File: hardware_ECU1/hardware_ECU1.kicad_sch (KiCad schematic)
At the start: 5 parts, among them J1 Micro_SD_Card, J2 VBAT circuit, U1 MPU-6050, U2 ESP32-WROOM-32

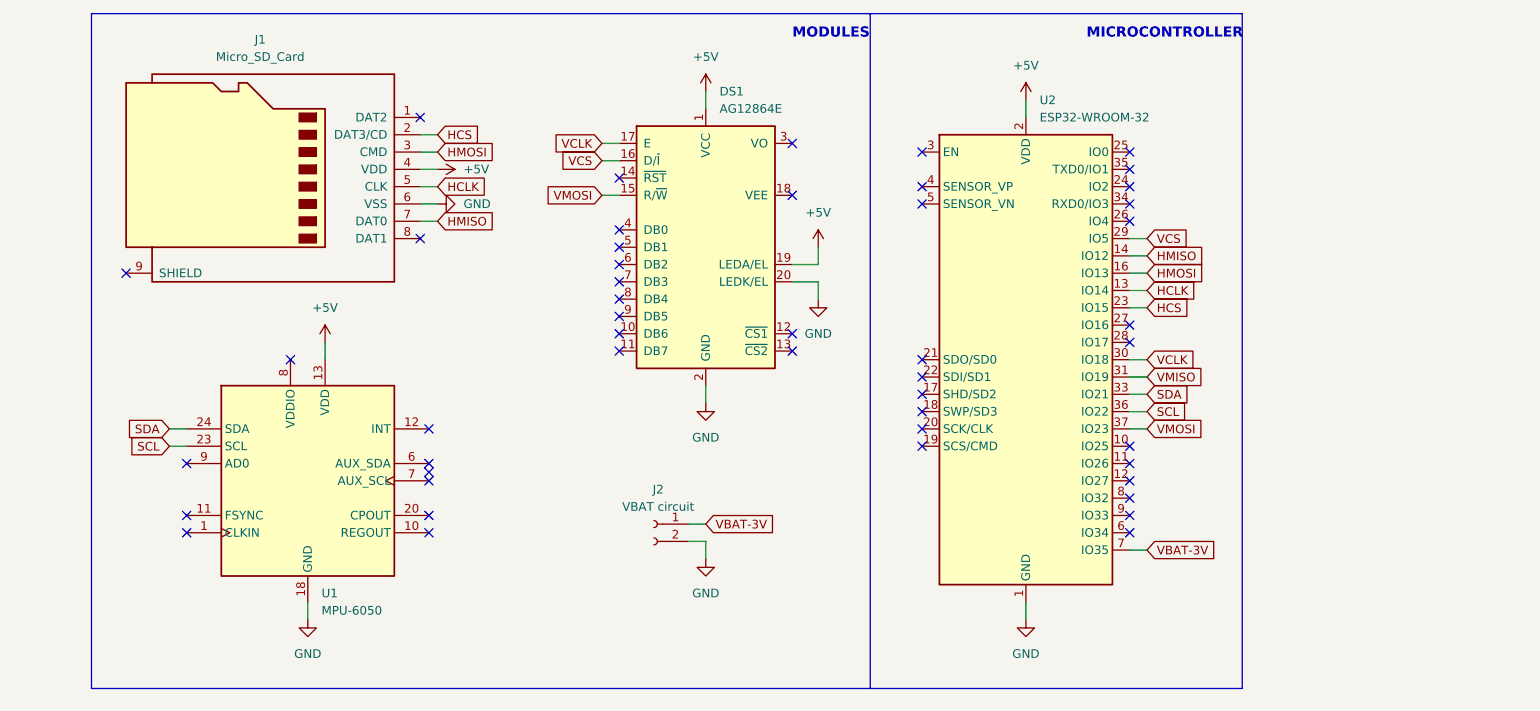
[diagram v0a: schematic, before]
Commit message: add buck to schematic
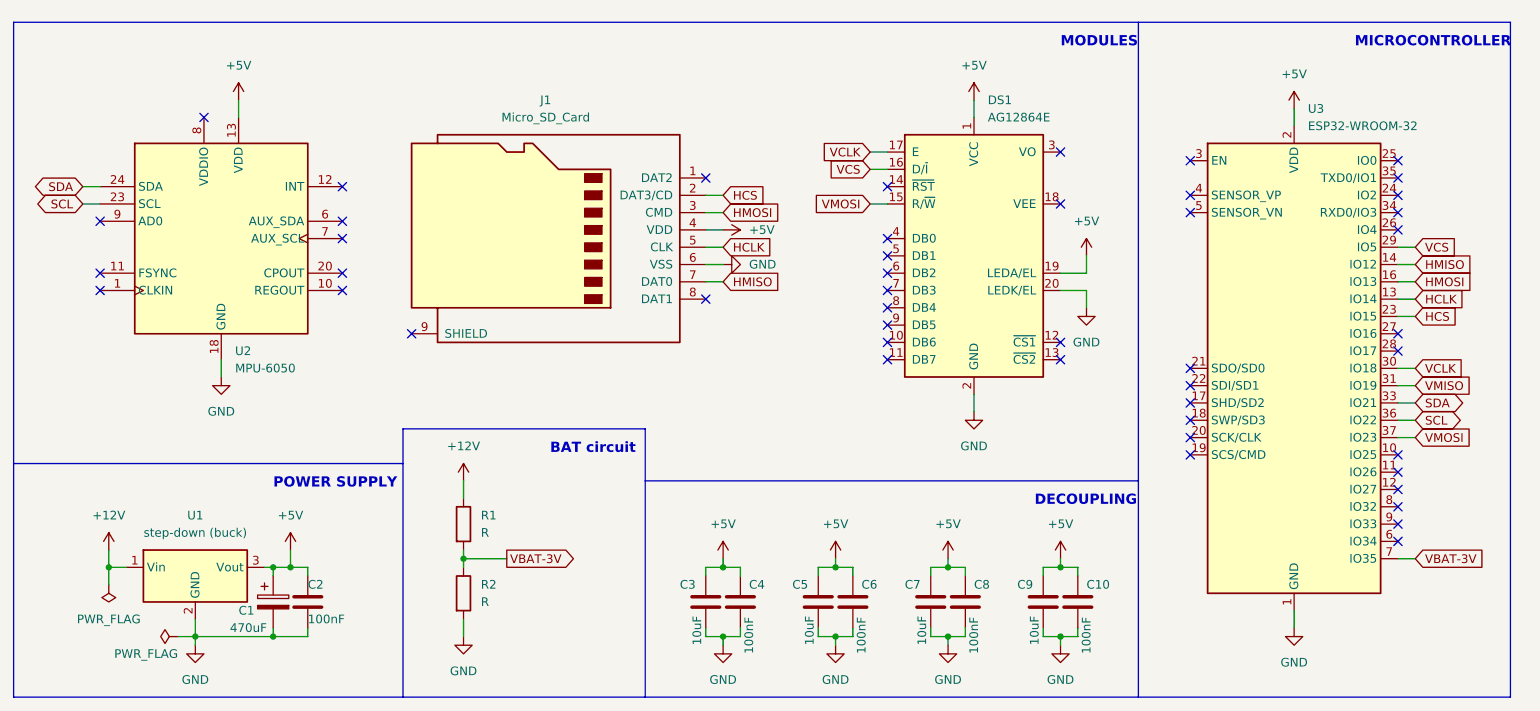
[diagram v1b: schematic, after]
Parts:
- removed J2: VBAT circuit, symbol Connector:Conn_01x02_Female
- added C1: 470uF, symbol Device:C_Polarized
- added C10, C2, C4, C6, C8: 100nF, symbol Device:C
- added C3, C5, C7, C9: 10uF, symbol Device:C
- added R1, R2: R, symbol Device:R
- added U1: step-down (buck), Converter_DCDC:Converter_DCDC_TRACO_TSR-1_THT, symbol Regulator_Switching:TSR_1-2412
- renumbered U1 to U2, U2 to U3
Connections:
- net +5V: now also C1.1, C10.1, C2.1, C3.1, C4.1, C5.1, C6.1, C7.1, C8.1, C9.1, U1.3 (Vout)
- net GND: now also C1.2, C10.2, C2.2, C3.2, C4.2, C5.2, C6.2, C7.2, C8.2, C9.2, R2.2, U1.2 (GND)
- net VBAT-3V: now also R1.2, R2.1
- new net +12V: R1.1, U1.1 (Vin)
- no-connect marks 48 -> 47
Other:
- note added: "BAT circuit"
- note added: "DECOUPLING"
- note added: "POWER SUPPLY"
- moved on the sheet: DS1, J1, U2, U3

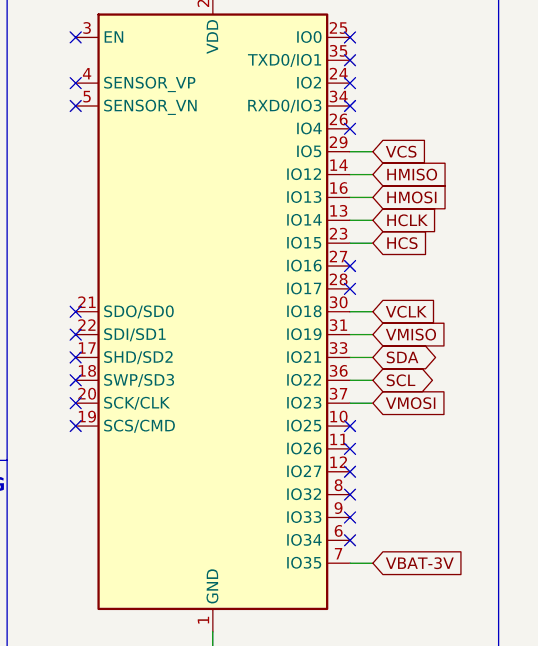
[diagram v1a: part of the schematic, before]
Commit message: fix HSPI pins
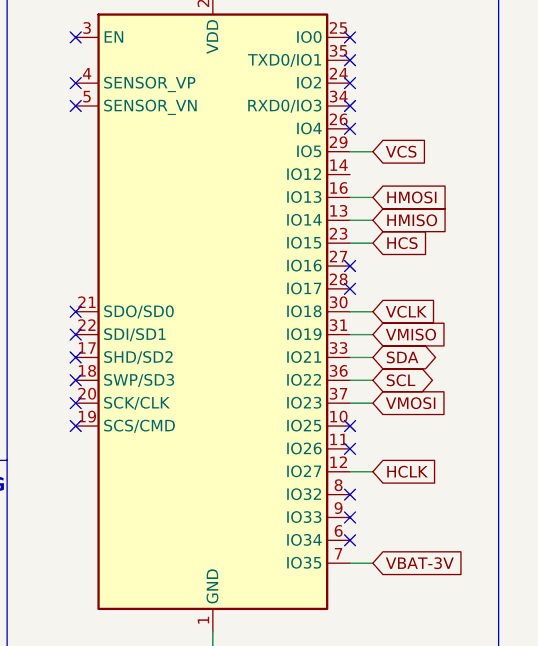
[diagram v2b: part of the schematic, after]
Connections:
- net HCLK: now also U3.12 (IO27); no longer U3.13 (IO14)
- net HMISO: now also U3.13 (IO14); no longer U3.14 (IO12)
- no-connect marks 47 -> 46
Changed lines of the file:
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@@
   (no_connect (at 243.84 115.57))
   (no_connect (at 243.84 125.73))
-  (no_connect (at 243.84 118.11))
   (no_connect (at 243.84 120.65))
   (no_connect (at 243.84 123.19))
@@
     (stroke (width 0) (type default) (color 0 0 0 0))
   )
-  (wire (pts (xy 243.84 85.09) (xy 246.38 85.09))
-    (stroke (width 0) (type default) (color 0 0 0 0))
-  )
   (wire (pts (xy 243.84 105.41) (xy 246.38 105.41))
     (stroke (width 0) (type default) (color 0 0 0 0))
@@
   )
   (wire (pts (xy 243.84 82.55) (xy 246.38 82.55))
+    (stroke (width 0) (type default) (color 0 0 0 0))
+  )
+  (wire (pts (xy 243.84 118.11) (xy 246.38 118.11))
     (stroke (width 0) (type default) (color 0 0 0 0))
   )
@@
     )
   )
-  (global_label "HMISO" (shape input) (at 246.38 85.09 0) (fields_autoplaced)
-    (effects (font (size 1.27 1.27)) (justify left))
-    (property "Intersheet References" "${INTERSHEET_REFS}" (id 0) (at 254.7198 85.0106 0)
+  (global_label "HMISO" (shape input) (at 246.38 90.17 0) (fields_autoplaced)
+    (effects (font (size 1.27 1.27)) (justify left))
+    (property "Intersheet References" "${INTERSHEET_REFS}" (id 0) (at 254.7198 90.0906 0)
       (effects (font (size 1.27 1.27)) (justify left) hide)
     )
@@
     )
   )
-  (global_label "HCLK" (shape input) (at 246.38 90.17 0) (fields_autoplaced)
-    (effects (font (size 1.27 1.27)) (justify left))
-    (property "Intersheet References" "${INTERSHEET_REFS}" (id 0) (at 253.6917 90.0906 0)
-      (effects (font (size 1.27 1.27)) (justify left) hide)
-    )
+  (global_label "HCLK" (shape input) (at 246.38 118.11 0) (fields_autoplaced)
+    (effects (font (size 1.27 1.27)) (justify left))
+    (property "Intersheet References" "${INTERSHEET_REFS}" (id 0) (at 253.6917 118.0306 0)
+      (effects (font (size 1.27 1.27)) (justify left) hide)
+    )

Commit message: Update hardware_ECU1.kicad_sch
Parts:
- removed C3, C5: 10uF, symbol Device:C
- removed C4, C6: 100nF, symbol Device:C
- added D1: LED, symbol Device:LED
- added R3: 470R, symbol Device:R
- R1: value R -> 10k
- R2: value R -> 2k2
- renumbered C7 to C3, C8 to C4, C9 to C5, C10 to C6
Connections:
- net GND: now also R3.2
- net HCS: now also U3.26 (IO4); no longer U3.23 (IO15)
- net LED_ALIVE: now reaches U3.14 (IO12)
- net LED_ALIVE: now also D1.1 (K)
- net VMISO: no longer names the net of U3.31 (IO19)
- new net: D1.2 (A), R3.1
- no-connect marks 46 -> 47
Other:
- note added: "ALIVE"

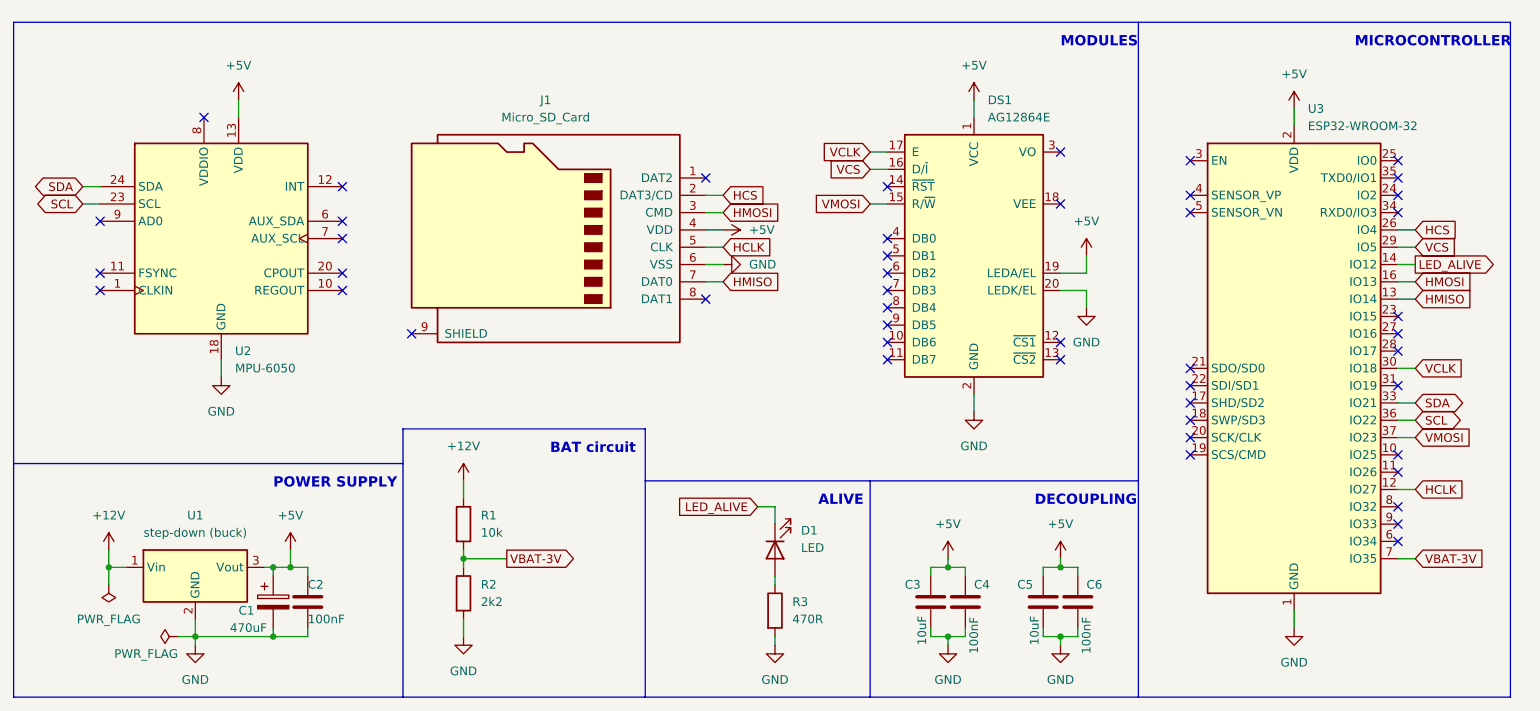
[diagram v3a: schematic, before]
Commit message: update display pins
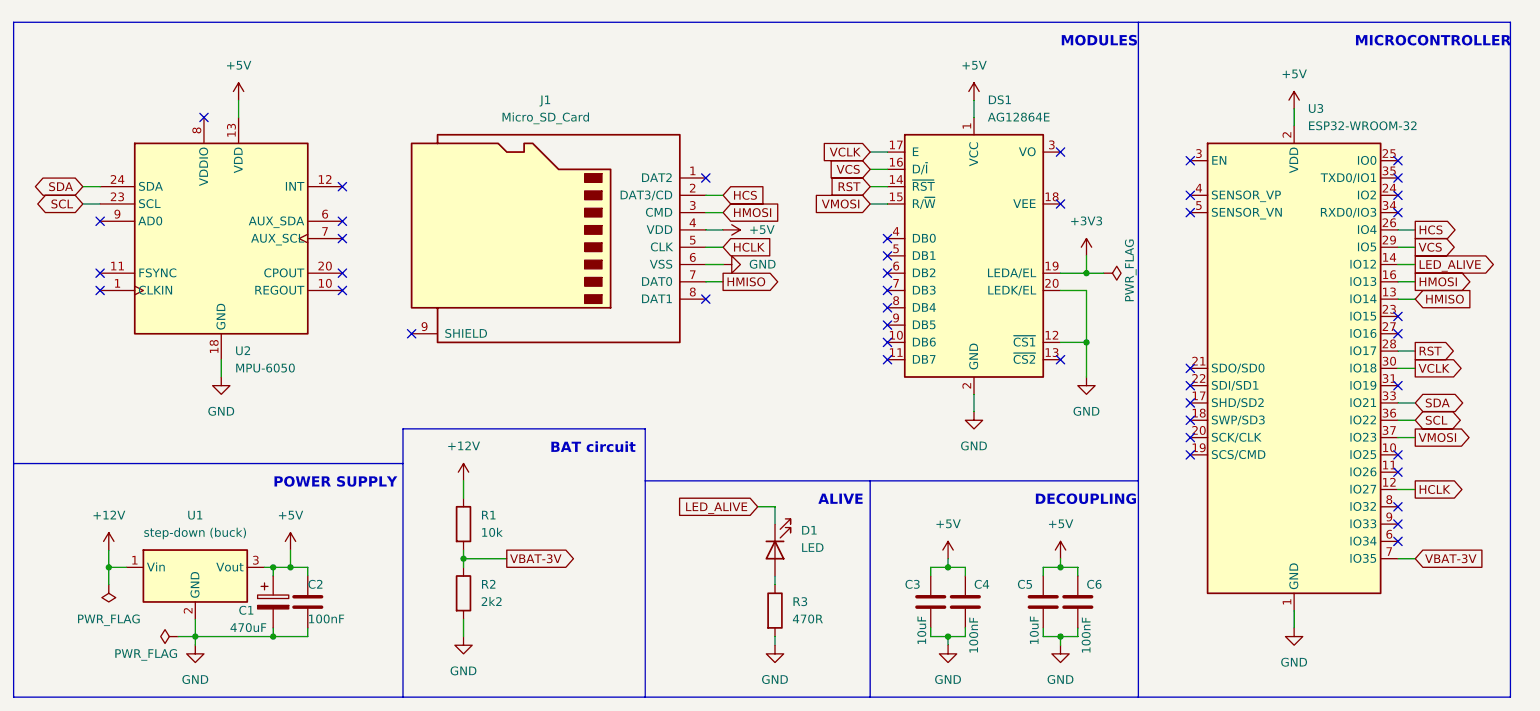
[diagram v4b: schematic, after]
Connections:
- net +5V: no longer DS1.19 (LEDA/EL)
- net GND: now also DS1.12 (~{CS1})
- net RST: now reaches DS1.14 (~{RST})
- net RST: now also U3.28 (IO17)
- new net +3V3: DS1.19 (LEDA/EL)
- no-connect marks 47 -> 44
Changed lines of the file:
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@@
   (junction (at 78.74 139.7) (diameter 0) (color 0 0 0 0)
   )
-  (no_connect (at 194.31 96.52))
+  (junction (at 198.12 96.52) (diameter 0) (color 0 0 0 0)
+  )
+  (junction (at 198.12 86.36) (diameter 0) (color 0 0 0 0)
+  )
   (no_connect (at 194.31 99.06))
   (no_connect (at 168.91 81.28))
   (no_connect (at 168.91 83.82))
   (no_connect (at 168.91 86.36))
-  (no_connect (at 168.91 73.66))
   (no_connect (at 194.31 76.2))
   (no_connect (at 168.91 99.06))
@@
   (no_connect (at 243.84 120.65))
   (no_connect (at 243.84 123.19))
-  (no_connect (at 243.84 97.79))
   (no_connect (at 243.84 95.25))
   (no_connect (at 243.84 92.71))
@@
     (stroke (width 0) (type default) (color 0 0 0 0))
   )
+  (wire (pts (xy 198.12 86.36) (xy 200.66 86.36))
+    (stroke (width 0) (type default) (color 0 0 0 0))
+  )
   (wire (pts (xy 243.84 85.09) (xy 246.38 85.09))
     (stroke (width 0) (type default) (color 0 0 0 0))
@@
     (stroke (width 0) (type default) (color 0 0 0 0))
   )
+  (wire (pts (xy 198.12 96.52) (xy 198.12 88.9))
+    (stroke (width 0) (type default) (color 0 0 0 0))
+  )
   (wire (pts (xy 194.31 140.97) (xy 194.31 139.7))
     (stroke (width 0) (type default) (color 0 0 0 0))
@@
     (stroke (width 0) (type default) (color 0 0 0 0))
   )
+  (wire (pts (xy 194.31 96.52) (xy 198.12 96.52))
+    (stroke (width 0) (type default) (color 0 0 0 0))
+  )
   (wire (pts (xy 83.82 130.81) (xy 83.82 129.54))
     (stroke (width 0) (type default) (color 0 0 0 0))
@@
     (stroke (width 0) (type default) (color 0 0 0 0))
   )
-  (wire (pts (xy 198.12 91.44) (xy 198.12 88.9))
+  (wire (pts (xy 198.12 101.6) (xy 198.12 96.52))
     (stroke (width 0) (type default) (color 0 0 0 0))
   )
@@
     (stroke (width 0) (type default) (color 0 0 0 0))
   )
+  (wire (pts (xy 243.84 97.79) (xy 246.38 97.79))
+    (stroke (width 0) (type default) (color 0 0 0 0))
+  )
   (wire (pts (xy 83.82 138.43) (xy 83.82 139.7))
     (stroke (width 0) (type default) (color 0 0 0 0))
@@
   )
   (wire (pts (xy 181.61 60.96) (xy 181.61 63.5))
+    (stroke (width 0) (type default) (color 0 0 0 0))
+  )
+  (wire (pts (xy 166.37 73.66) (xy 168.91 73.66))
     (stroke (width 0) (type default) (color 0 0 0 0))
   )
@@
     )
   )
-  (global_label "HMOSI" (shape input) (at 246.38 87.63 0) (fields_autoplaced)
+  (global_label "HMOSI" (shape output) (at 246.38 87.63 0) (fields_autoplaced)
     (effects (font (size 1.27 1.27)) (justify left))
     (property "Intersheet References" "${INTERSHEET_REFS}" (id 0) (at 254.7198 87.5506 0)
@@
     )
   )
-  (global_label "HCLK" (shape input) (at 246.38 118.11 0) (fields_autoplaced)
+  (global_label "HCLK" (shape output) (at 246.38 118.11 0) (fields_autoplaced)
     (effects (font (size 1.27 1.27)) (justify left))
     (property "Intersheet References" "${INTERSHEET_REFS}" (id 0) (at 253.6917 118.0306 0)
@@
     )
   )
-  (global_label "VCLK" (shape input) (at 246.38 100.33 0) (fields_autoplaced)
+  (global_label "RST" (shape input) (at 166.37 73.66 180) (fields_autoplaced)
+    (effects (font (size 1.27 1.27)) (justify right))
+    (property "Intersheet References" "${INTERSHEET_REFS}" (id 0) (at 160.5098 73.5806 0)
+      (effects (font (size 1.27 1.27)) (justify right) hide)
+    )
+  )
+  (global_label "VCLK" (shape output) (at 246.38 100.33 0) (fields_autoplaced)
     (effects (font (size 1.27 1.27)) (justify left))
     (property "Intersheet References" "${INTERSHEET_REFS}" (id 0) (at 253.4498 100.2506 0)
@@
     )
   )
-  (global_label "HCS" (shape input) (at 246.38 80.01 0) (fields_autoplaced)
+  (global_label "HCS" (shape output) (at 246.38 80.01 0) (fields_autoplaced)
     (effects (font (size 1.27 1.27)) (justify left))
     (property "Intersheet References" "${INTERSHEET_REFS}" (id 0) (at 252.6031 79.9306 0)
@@
     )
   )
+  (global_label "RST" (shape output) (at 246.38 97.79 0) (fields_autoplaced)
+    (effects (font (size 1.27 1.27)) (justify left))
+    (property "Intersheet References" "${INTERSHEET_REFS}" (id 0) (at 252.2402 97.7106 0)
+      (effects (font (size 1.27 1.27)) (justify left) hide)
+    )
+  )
   (global_label "HCS" (shape input) (at 144.78 74.93 0) (fields_autoplaced)
     (effects (font (size 1.27 1.27)) (justify left))
@@
     )
   )
-  (global_label "VMOSI" (shape input) (at 246.38 110.49 0) (fields_autoplaced)
+  (global_label "VMOSI" (shape output) (at 246.38 110.49 0) (fields_autoplaced)
     (effects (font (size 1.27 1.27)) (justify left))
     (property "Intersheet References" "${INTERSHEET_REFS}" (id 0) (at 254.4779 110.4106 0)
@@
     )
   )
-  (global_label "VCS" (shape input) (at 246.38 82.55 0) (fields_autoplaced)
+  (global_label "VCS" (shape output) (at 246.38 82.55 0) (fields_autoplaced)
     (effects (font (size 1.27 1.27)) (justify left))
     (property "Intersheet References" "${INTERSHEET_REFS}" (id 0) (at 252.3612 82.4706 0)
@@
     )
   )
-  (global_label "HMISO" (shape input) (at 144.78 87.63 0) (fields_autoplaced)
+  (global_label "HMISO" (shape output) (at 144.78 87.63 0) (fields_autoplaced)
     (effects (font (size 1.27 1.27)) (justify left))
     (property "Intersheet References" "${INTERSHEET_REFS}" (id 0) (at 153.1198 87.5506 0)
       (effects (font (size 1.27 1.27)) (justify left) hide)
     )
+  )
+  (symbol (lib_id "power:+3V3") (at 198.12 83.82 0) (unit 1)
+    (in_bom yes) (on_board yes) (fields_autoplaced)
+    (property "Reference" "#PWR017" (id 0) (at 198.12 87.63 0)
+      (effects (font (size 1.27 1.27)) hide)
+    )
+    (property "Value" "+3V3" (id 1) (at 198.12 78.74 0))
+    (property "Footprint" "" (id 2) (at 198.12 83.82 0)
+      (effects (font (size 1.27 1.27)) hide)
+    )
+    (property "Datasheet" "" (id 3) (at 198.12 83.82 0)
+      (effects (font (size 1.27 1.27)) hide)
+    )
+    (pin "1")
   )
   (symbol (lib_id "power:PWR_FLAG") (at 64.77 139.7 90) (unit 1)
@@
     (pin "1")
   )
-  (symbol (lib_id "power:GND") (at 198.12 91.44 0) (unit 1)
-    (in_bom yes) (on_board yes) (fields_autoplaced)
-    (property "Reference" "#PWR018" (id 0) (at 198.12 97.79 0)
-      (effects (font (size 1.27 1.27)) hide)
-    )
-    (property "Value" "GND" (id 1) (at 198.12 96.52 0))
-    (property "Footprint" "" (id 2) (at 198.12 91.44 0)
-      (effects (font (size 1.27 1.27)) hide)
-    )
-    (property "Datasheet" "" (id 3) (at 198.12 91.44 0)
+  (symbol (lib_id "power:GND") (at 198.12 101.6 0) (unit 1)
+    (in_bom yes) (on_board yes) (fields_autoplaced)
+    (property "Reference" "#PWR018" (id 0) (at 198.12 107.95 0)
+      (effects (font (size 1.27 1.27)) hide)
+    )
+    (property "Value" "GND" (id 1) (at 198.12 106.68 0))
+    (property "Footprint" "" (id 2) (at 198.12 101.6 0)
+      (effects (font (size 1.27 1.27)) hide)
+    )
+    (property "Datasheet" "" (id 3) (at 198.12 101.6 0)
       (effects (font (size 1.27 1.27)) hide)
     )
@@
     (pin "1")
   )
-  (symbol (lib_id "power:+5V") (at 198.12 83.82 0) (unit 1)
-    (in_bom yes) (on_board yes) (fields_autoplaced)
-    (property "Reference" "#PWR017" (id 0) (at 198.12 87.63 0)
-      (effects (font (size 1.27 1.27)) hide)
-    )
-    (property "Value" "+5V" (id 1) (at 198.12 78.74 0))
-    (property "Footprint" "" (id 2) (at 198.12 83.82 0)
-      (effects (font (size 1.27 1.27)) hide)
-    )
-    (property "Datasheet" "" (id 3) (at 198.12 83.82 0)
+  (symbol (lib_id "power:PWR_FLAG") (at 200.66 86.36 270) (unit 1)
+    (in_bom yes) (on_board yes)
+    (property "Reference" "#FLG0101" (id 0) (at 202.565 86.36 0)
+      (effects (font (size 1.27 1.27)) hide)
+    )
+    (property "Value" "PWR_FLAG" (id 1) (at 204.47 81.28 0)
+      (effects (font (size 1.27 1.27)) (justify left))
+    )
+    (property "Footprint" "" (id 2) (at 200.66 86.36 0)
+      (effects (font (size 1.27 1.27)) hide)
+    )
+    (property "Datasheet" "~" (id 3) (at 200.66 86.36 0)
       (effects (font (size 1.27 1.27)) hide)
     )
@@
       (reference "#FLG02") (unit 1) (value "PWR_FLAG") (footprint "")
     )
+    (path "/78c58950-0050-4443-94fc-285094f433b5"
+      (reference "#FLG0101") (unit 1) (value "PWR_FLAG") (footprint "")
+    )
     (path "/e6716b01-b543-48cf-afc3-e4e381c816d9"
       (reference "#PWR01") (unit 1) (value "+12V") (footprint "")
@@
       (reference "#PWR016") (unit 1) (value "GND") (footprint "")
     )
-    (path "/7e6d2e7b-d08b-45bb-a567-c474be30f298"
-      (reference "#PWR017") (unit 1) (value "+5V") (footprint "")
+    (path "/00673137-96e6-46f4-a26f-9b2ff4530aff"
+      (reference "#PWR017") (unit 1) (value "+3V3") (footprint "")
     )
     (path "/3c439122-d9c0-4b66-9e04-931ad0c7959f"
